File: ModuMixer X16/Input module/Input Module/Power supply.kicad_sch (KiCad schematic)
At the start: 28 parts, among them Q2 IRF9540N, Q3 MMBT2222A, U6 LM317_TO-220, U7 LM317_TO-220

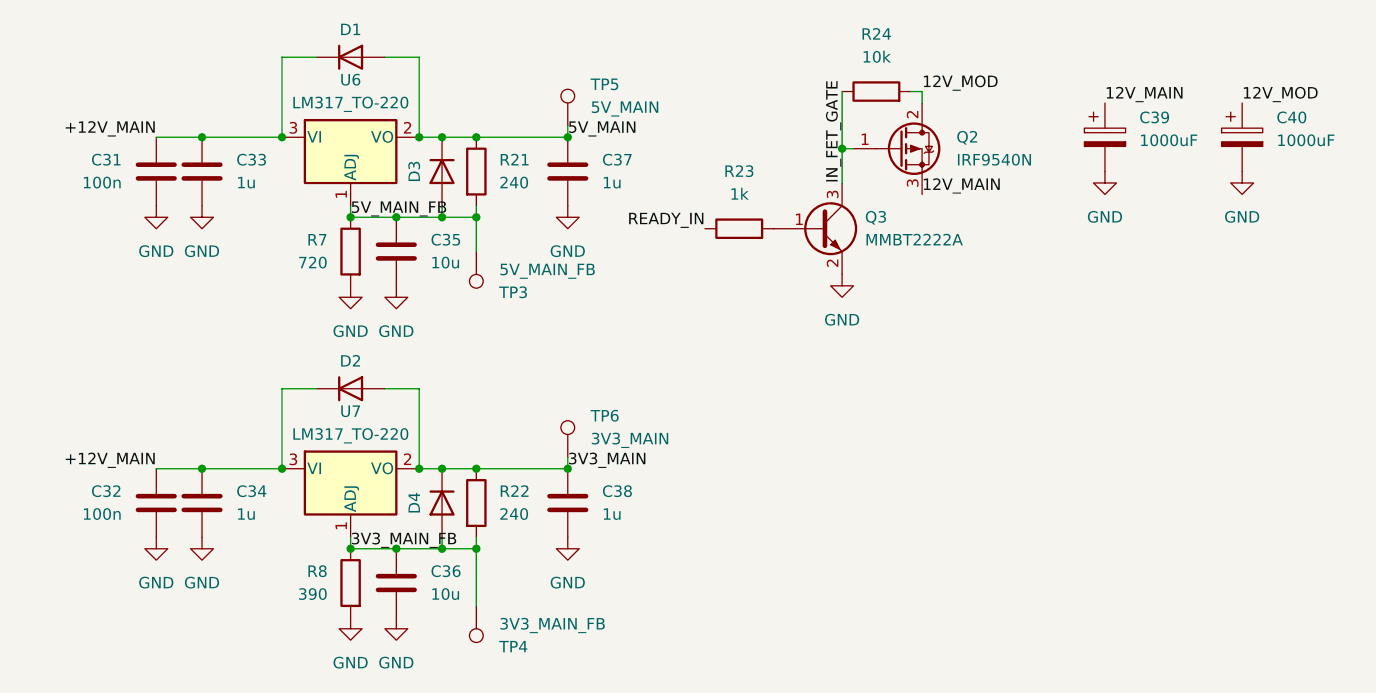
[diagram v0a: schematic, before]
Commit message: MCU replacement finished
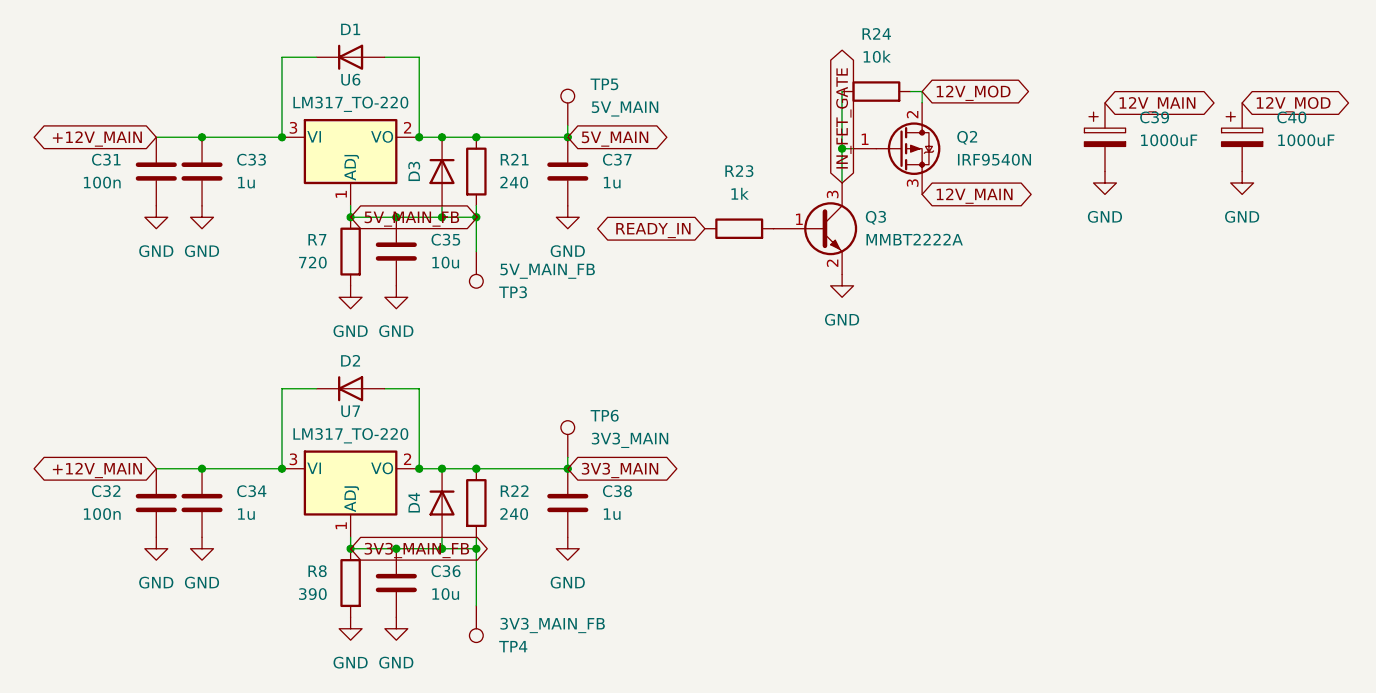
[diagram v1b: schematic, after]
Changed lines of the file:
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@@
 		)
 	)
-	(label "READY_IN"
+	(global_label "READY_IN"
+		(shape bidirectional)
 		(at 88.9 38.1 180)
 		(fields_autoplaced yes)
@@
 			(justify right bottom)
 		)
-	)
-	(label "+12V_MAIN"
+		(property "Intersheetrefs" "${INTERSHEET_REFS}"
+			(at 88.9 38.1 0)
+			(effects
+				(font
+					(size 1.27 1.27)
+				)
+				(hide yes)
+			)
+		)
+	)
+	(global_label "+12V_MAIN"
+		(shape bidirectional)
 		(at 27.94 27.94 180)
 		(fields_autoplaced yes)
@@
 			(justify right bottom)
 		)
-	)
-	(label "5V_MAIN_FB"
+		(property "Intersheetrefs" "${INTERSHEET_REFS}"
+			(at 27.94 27.94 0)
+			(effects
+				(font
+					(size 1.27 1.27)
+				)
+				(hide yes)
+			)
+		)
+	)
+	(global_label "5V_MAIN_FB"
+		(shape bidirectional)
 		(at 49.53 36.83 0)
 		(fields_autoplaced yes)
@@
 			(justify left bottom)
 		)
-	)
-	(label "3V3_MAIN_FB"
+		(property "Intersheetrefs" "${INTERSHEET_REFS}"
+			(at 49.53 36.83 0)
+			(effects
+				(font
+					(size 1.27 1.27)
+				)
+				(hide yes)
+			)
+		)
+	)
+	(global_label "3V3_MAIN_FB"
+		(shape bidirectional)
 		(at 49.53 73.66 0)
 		(fields_autoplaced yes)
@@
 			(justify left bottom)
 		)
-	)
-	(label "IN_FET_GATE"
+		(property "Intersheetrefs" "${INTERSHEET_REFS}"
+			(at 49.53 73.66 0)
+			(effects
+				(font
+					(size 1.27 1.27)
+				)
+				(hide yes)
+			)
+		)
+	)
+	(global_label "IN_FET_GATE"
+		(shape bidirectional)
 		(at 104.14 33.02 90)
 		(fields_autoplaced yes)
@@
 			(justify left bottom)
 		)
-	)
-	(label "12V_MAIN"
+		(property "Intersheetrefs" "${INTERSHEET_REFS}"
+			(at 104.14 33.02 0)
+			(effects
+				(font
+					(size 1.27 1.27)
+				)
+				(hide yes)
+			)
+		)
+	)
+	(global_label "12V_MAIN"
+		(shape bidirectional)
 		(at 113.03 34.29 0)
 		(fields_autoplaced yes)
@@
 			(justify left bottom)
 		)
-	)
-	(label "+12V_MAIN"
+		(property "Intersheetrefs" "${INTERSHEET_REFS}"
+			(at 113.03 34.29 0)
+			(effects
+				(font
+					(size 1.27 1.27)
+				)
+				(hide yes)
+			)
+		)
+	)
+	(global_label "+12V_MAIN"
+		(shape bidirectional)
 		(at 27.94 64.77 180)
 		(fields_autoplaced yes)
@@
 			(justify right bottom)
 		)
-	)
-	(label "5V_MAIN"
+		(property "Intersheetrefs" "${INTERSHEET_REFS}"
+			(at 27.94 64.77 0)
+			(effects
+				(font
+					(size 1.27 1.27)
+				)
+				(hide yes)
+			)
+		)
+	)
+	(global_label "5V_MAIN"
+		(shape bidirectional)
 		(at 73.66 27.94 0)
 		(fields_autoplaced yes)
@@
 			(justify left bottom)
 		)
-	)
-	(label "12V_MAIN"
+		(property "Intersheetrefs" "${INTERSHEET_REFS}"
+			(at 73.66 27.94 0)
+			(effects
+				(font
+					(size 1.27 1.27)
+				)
+				(hide yes)
+			)
+		)
+	)
+	(global_label "12V_MAIN"
+		(shape bidirectional)
 		(at 133.35 24.13 0)
 		(fields_autoplaced yes)
@@
 			(justify left bottom)
 		)
-	)
-	(label "12V_MOD"
+		(property "Intersheetrefs" "${INTERSHEET_REFS}"
+			(at 133.35 24.13 0)
+			(effects
+				(font
+					(size 1.27 1.27)
+				)
+				(hide yes)
+			)
+		)
+	)
+	(global_label "12V_MOD"
+		(shape bidirectional)
 		(at 113.03 22.86 0)
 		(fields_autoplaced yes)
@@
 			(justify left bottom)
 		)
-	)
-	(label "3V3_MAIN"
+		(property "Intersheetrefs" "${INTERSHEET_REFS}"
+			(at 113.03 22.86 0)
+			(effects
+				(font
+					(size 1.27 1.27)
+				)
+				(hide yes)
+			)
+		)
+	)
+	(global_label "3V3_MAIN"
+		(shape bidirectional)
 		(at 73.66 64.77 0)
 		(fields_autoplaced yes)
@@
 			(justify left bottom)
 		)
-	)
-	(label "12V_MOD"
+		(property "Intersheetrefs" "${INTERSHEET_REFS}"
+			(at 73.66 64.77 0)
+			(effects
+				(font
+					(size 1.27 1.27)
+				)
+				(hide yes)
+			)
+		)
+	)
+	(global_label "12V_MOD"
+		(shape bidirectional)
 		(at 148.59 24.13 0)
 		(fields_autoplaced yes)
@@
 			(justify left bottom)
 		)
+		(property "Intersheetrefs" "${INTERSHEET_REFS}"
+			(at 148.59 24.13 0)
+			(effects
+				(font
+					(size 1.27 1.27)
+				)
+				(hide yes)
+			)
+		)
 	)
 	(symbol
@@
 			)
 		)
-		(property "Description" "Power symbol creates a global label with name \"GND\" , ground"
+		(property "Description" "Power symbol creates a global global_label with name \"GND\" , ground"
 			(at 73.66 72.39 0)
 			(effects
@@
 			)
 		)
-		(property "Description" "Power symbol creates a global label with name \"GND\" , ground"
+		(property "Description" "Power symbol creates a global global_label with name \"GND\" , ground"
 			(at 27.94 72.39 0)
 			(effects
@@
 			)
 		)
-		(property "Description" "Power symbol creates a global label with name \"GND\" , ground"
+		(property "Description" "Power symbol creates a global global_label with name \"GND\" , ground"
 			(at 33.02 35.56 0)
 			(effects
@@
 			)
 		)
-		(property "Description" "Power symbol creates a global label with name \"GND\" , ground"
+		(property "Description" "Power symbol creates a global global_label with name \"GND\" , ground"
 			(at 49.53 81.28 0)
 			(effects
@@
 			)
 		)
-		(property "Description" "Power symbol creates a global label with name \"GND\" , ground"
+		(property "Description" "Power symbol creates a global global_label with name \"GND\" , ground"
 			(at 27.94 35.56 0)
 			(effects
@@
 			)
 		)
-		(property "Description" "Power symbol creates a global label with name \"GND\" , ground"
+		(property "Description" "Power symbol creates a global global_label with name \"GND\" , ground"
 			(at 49.53 44.45 0)
 			(effects
@@
 			)
 		)
-		(property "Description" "Power symbol creates a global label with name \"GND\" , ground"
+		(property "Description" "Power symbol creates a global global_label with name \"GND\" , ground"
 			(at 133.35 31.75 0)
 			(effects
@@
 			)
 		)
-		(property "Description" "Power symbol creates a global label with name \"GND\" , ground"
+		(property "Description" "Power symbol creates a global global_label with name \"GND\" , ground"
 			(at 54.61 44.45 0)
 			(effects
@@
 			)
 		)
-		(property "Description" "Power symbol creates a global label with name \"GND\" , ground"
+		(property "Description" "Power symbol creates a global global_label with name \"GND\" , ground"
 			(at 54.61 81.28 0)
 			(effects
@@
 			)
 		)
-		(property "Description" "Power symbol creates a global label with name \"GND\" , ground"
+		(property "Description" "Power symbol creates a global global_label with name \"GND\" , ground"
 			(at 148.59 31.75 0)
 			(effects
@@
 			)
 		)
-		(property "Description" "Power symbol creates a global label with name \"GND\" , ground"
+		(property "Description" "Power symbol creates a global global_label with name \"GND\" , ground"
 			(at 104.14 43.18 0)
 			(effects
@@
 			)
 		)
-		(property "Description" "Power symbol creates a global label with name \"GND\" , ground"
+		(property "Description" "Power symbol creates a global global_label with name \"GND\" , ground"
 			(at 33.02 72.39 0)
 			(effects
@@
 			)
 		)
-		(property "Description" "Power symbol creates a global label with name \"GND\" , ground"
+		(property "Description" "Power symbol creates a global global_label with name \"GND\" , ground"
 			(at 73.66 35.56 0)
 			(effects
